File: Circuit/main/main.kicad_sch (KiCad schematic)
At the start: 19 parts

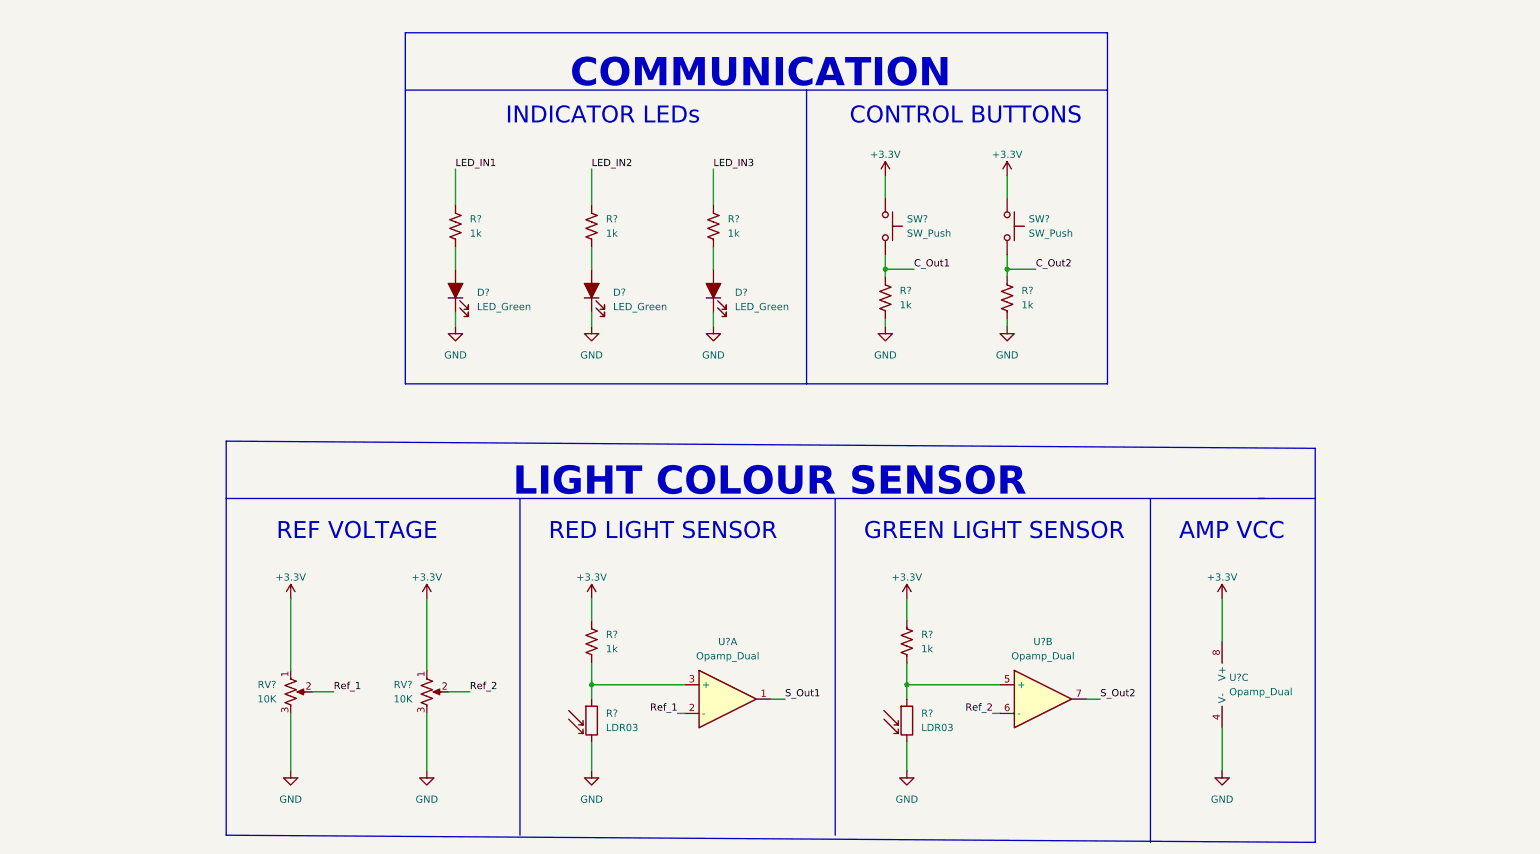
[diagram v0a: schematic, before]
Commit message: Added 3.3V voltage regulator
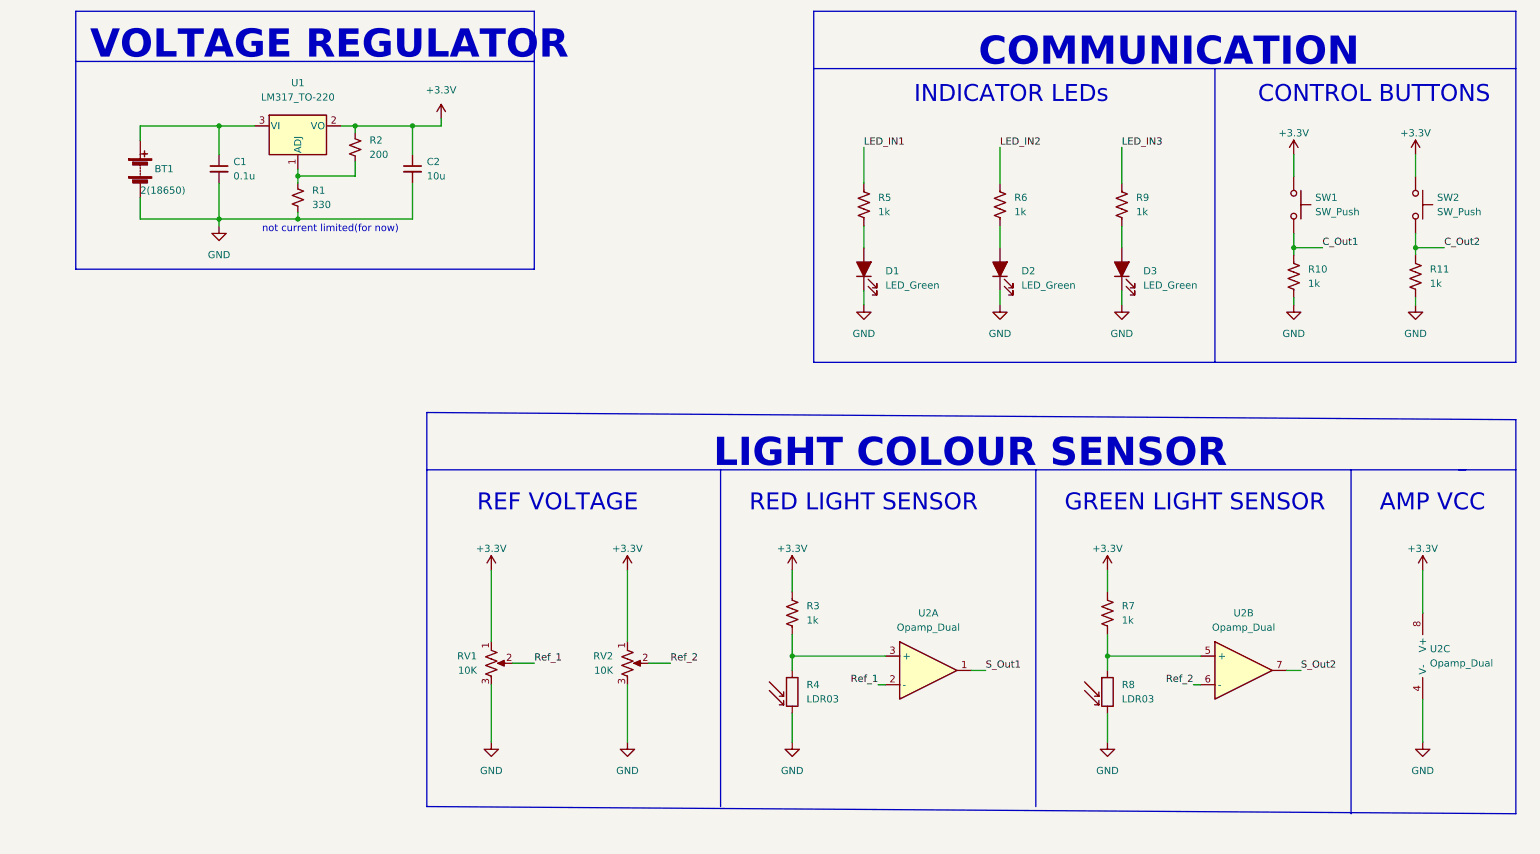
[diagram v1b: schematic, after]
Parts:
- added BT1: 2(18650), symbol Device:Battery
- added C1: 0.1u, symbol Device:C_Small
- added C2: 10u, symbol Device:C_Small
- added R1: 330, symbol Device:R_Small_US
- added R2: 200, symbol Device:R_Small_US
- added U1: LM317_TO-220, Package_TO_SOT_THT:TO-220-3_Vertical, symbol Regulator_Linear:LM317_TO-220
- gave numbers to parts that had none: 17
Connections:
- net +3V3: now also C2.1, R2.1, U1.2 (VO)
- net GND: now also BT1.2 (-), C1.2, C2.2, R1.2
- new net: R1.1, R2.2, U1.1 (ADJ)
- new net: BT1.1 (+), C1.1, U1.3 (VI)
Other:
- note added: "VOLTAGE REGULATOR"
- note added: "not current limited(for now)"
- moved on the sheet: D1, D2, D3, R10, R11, R3, R4, R5, R6, R7, R8, R9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

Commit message: Added 2 logic shifters for red and green color detection
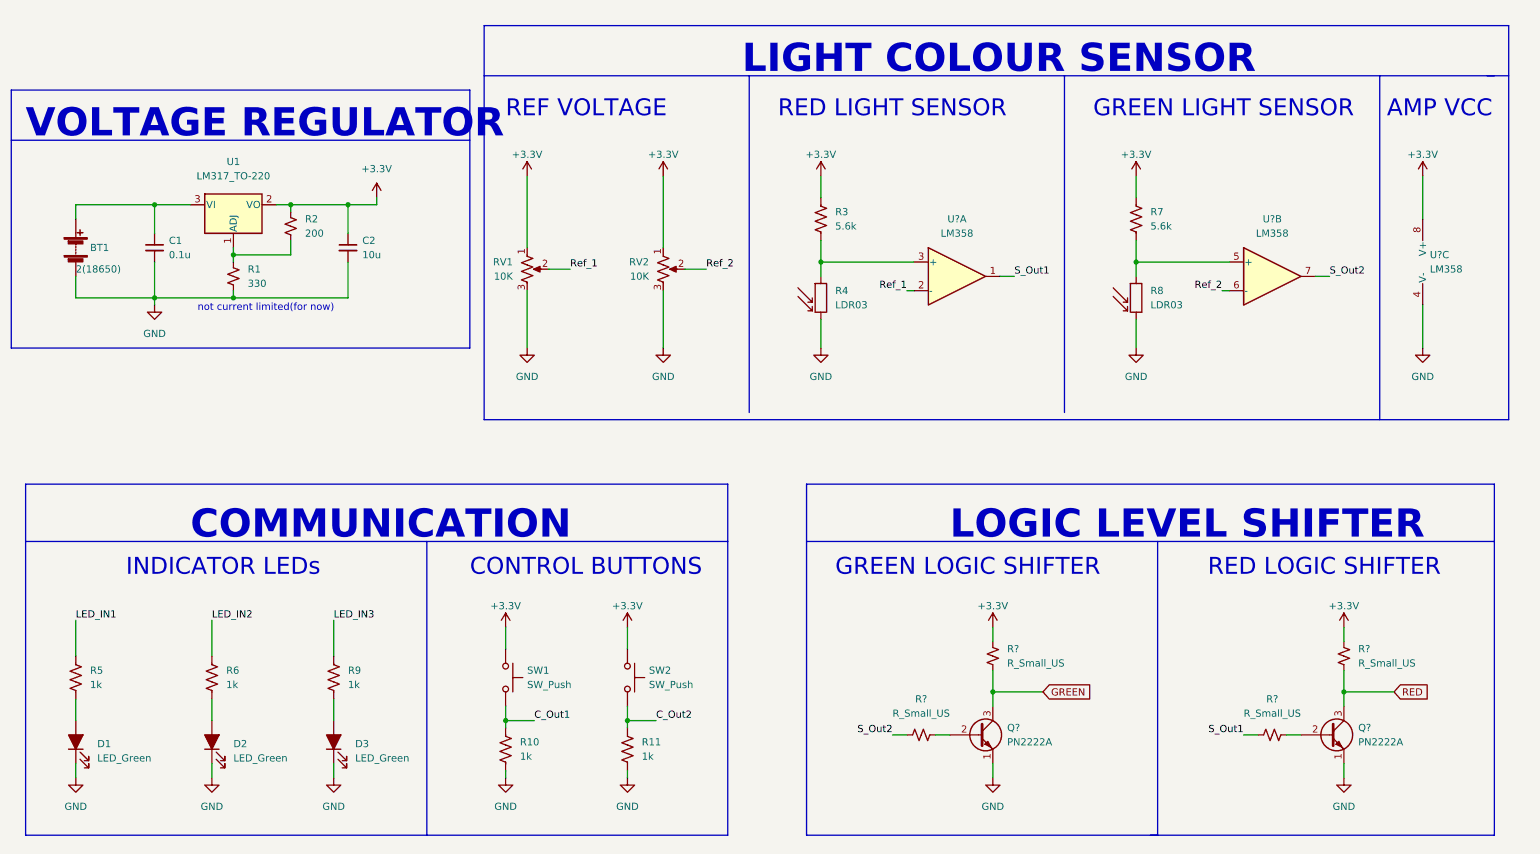
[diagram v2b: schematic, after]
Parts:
- removed U2: Opamp_Dual, symbol Device:Opamp_Dual
- added Q? (x2): PN2222A, Package_TO_SOT_THT:TO-92_Inline, symbol Transistor_BJT:PN2222A
- added R? (x4): R_Small_US, symbol Device:R_Small_US
- added U? (x3): LM358, symbol Amplifier_Operational:LM358
- R3, R7: value 1k -> 5.6k
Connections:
- net +3V3: now also R?.1, R?.1, U?.8 (V+)
- net GND: now also Q?.1 (E), Q?.1 (E), U?.4 (V-)
- net Ref_1: now also U?.2 (-)
- net Ref_2: now also U?.6 (-)
- net S_Out1: now also R?.1, U?.1
- net S_Out2: now also R?.1, U?.7
- net at R3.2, R4.1: now also U?.3 (+)
- net at R7.2, R8.1: now also U?.5 (+)
- new net: Q?.2 (B), R?.2 (x2)
- new net GREEN: Q?.3 (C), R?.2
- new net RED: Q?.3 (C), R?.2
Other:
- note added: "GREEN LOGIC SHIFTER"
- note added: "LOGIC LEVEL SHIFTER"
- note added: "RED LOGIC SHIFTER"
- moved on the sheet: BT1, C1, C2, D1, D2, D3, R1, R10, R11, R2, R3, R4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
